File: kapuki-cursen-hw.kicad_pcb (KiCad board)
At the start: 2 copper layers, 27 parts, among them J1 Conn_01x02, J2 Conn_01x02, J3 Conn_01x01, J4 Conn_01x01, J5 Conn_01x01, J6 Conn_01x01, J7 Conn_01x06, J8 Conn_01x05, U1 MIC5235, U2 MAX4081S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

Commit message: Routing rev.1
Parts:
- removed the R5 at (154.5, 91.3)
- added D3: LED, LED_SMD:LED_0402_1005Metric, F.Cu at (139.5, 61.9)
- added D4: BZT52H-C3V3, Diode_SMD:D_SOD-123F, F.Cu at (130.2, 66.5)
- added R3: R, Resistor_SMD:R_0402_1005Metric, F.Cu at (139.0, 63.6)
- added R6: R, Resistor_SMD:R_0402_1005Metric, F.Cu at (141.0, 65.0)
- added REF**: OSHW-Logo2_7.3x6mm_SilkScreen, Symbol:OSHW-Logo2_7.3x6mm_SilkScreen, F.Cu at (125.9, 55.8)
- R2: footprint Resistor_SMD:R_0201_0603Metric -> Resistor_SMD:R_0402_1005Metric
- R4: renamed from R3; footprint Resistor_SMD:R_0201_0603Metric -> Resistor_SMD:R_0402_1005Metric
- R5: renamed from R4; footprint Resistor_SMD:R_0201_0603Metric -> Resistor_SMD:R_0402_1005Metric
- moved C5 37.4 mm to (129.7, 61.7), turned to 90 degrees
- moved R5 34.7 mm to (143.5, 63.4), turned to 270 degrees
- moved C4 32.9 mm to (130.8, 61.7), turned to 90 degrees
- moved R4 29.7 mm to (143.5, 66.0), turned to 270 degrees
- moved C7 29.7 mm to (135.9, 67.7), turned to 180 degrees
- moved FB1 29.0 mm to (137.4, 68.8)
- moved D2 28.5 mm to (134.4, 59.2)
- moved C3 27.7 mm to (133.0, 57.4)
- moved R2 27.7 mm to (136.3, 57.4)
- moved U2 27.6 mm to (134.6, 55.0)
- moved C8 27.5 mm to (135.4, 68.8), turned to 180 degrees
- moved J5 26.6 mm to (146.2, 62.9)
- moved C6 26.2 mm to (138.4, 66.1), turned to 270 degrees
- moved J1 25.6 mm to (124.5, 54.4), turned to 0 degrees
- moved J2 25.6 mm to (144.8, 54.4), turned to 0 degrees
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- renumbered J3 to Je
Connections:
- net /VCC renamed VCC
- C7 pad 1: Net-(C7-Pad1) -> /VCCA
- C8 pad 1: Net-(C7-Pad1) -> /VCCA
- FB1 pad 1: Net-(C7-Pad1) -> /VCCA
- R1 pad 3: (no net) -> Net-(R1-Pad3)
- R1 pad 4: (no net) -> Net-(J2-Pad2)
- U3 pad 15: Net-(U3-Pad15) -> /VCCA
- U3 pad 21: Net-(U3-Pad21) -> /LED
- U3 pad 23: Net-(U3-Pad23) -> /SWCLK
- U3 pad 24: /SWCLK -> /SWDIO
- U3 pad 25: /SWDIO -> Net-(U3-Pad25)
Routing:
- net VCC: track 0.00 -> 41.7 mm, vias 0 -> 3
- net /CURRMEAS: track 0.00 -> 29.3 mm, vias 0 -> 2
- net /VREF: track 0.00 -> 27.1 mm, vias 0 -> 2
- net GND: track 0.00 -> 23.6 mm, vias 0 -> 8
- net Net-(D4-Pad1): track 0.00 -> 21.8 mm, vias 0 -> 2
- net /SWDIO: track 0.00 -> 21.6 mm, vias 0 -> 2
- net /SWCLK: track 0.00 -> 20.0 mm, vias 0 -> 2
- net /MOTORPULSE: track 0.00 -> 14.9 mm
- net /VCCIN: track 0.00 -> 13.2 mm
- net /RXTX: track 0.00 -> 12.1 mm
- net /EXT6: track 0.00 -> 9.47 mm
- net /EXT5: track 0.00 -> 8.35 mm
- net /EXT1: track 0.00 -> 7.60 mm
- net /EXT2: track 0.00 -> 6.39 mm
- net /EXT4: track 0.00 -> 6.34 mm
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- added copper zone on B.Cu, net GND
- added copper zone on F.Cu, net GND
- added copper zone on B.Cu, net Net-(J1-Pad2)
- added copper zone on B.Cu, net Net-(J2-Pad2)
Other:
- board outline added: 26.9 x 26.5 mm
- net class Default: clearance 0.2 -> 0.1524; trace_width 0.25 -> 0.1524; via_dia 0.8 -> 0.6858; via_drill 0.4 -> 0.3302
- net class VCC added: clearance 0.2032, trace_width 0.254, via_dia 0.6858, via_drill 0.3302
- rule pad_to_mask_clearance: 0.051 -> 0.0508
- rule solder_mask_min_width: 0.25 -> 0.0508
- rule trace_clearance: 0.2 -> 0.1524
- rule trace_min: 0.2 -> 0.1524
- rule via_min_drill: 0.3 -> 0.3302
- rule via_min_size: 0.4 -> 0.6858
- board text added: "SWD"

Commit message: Send to OSHPark
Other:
- board text added: "Current Sensor rev.1 1946"
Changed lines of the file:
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@@
   (general
     (thickness 1.6)
-    (drawings 8)
+    (drawings 9)
     (tracks 222)
     (zones 0)
@@
     (visible_elements FFFFFF7F)
     (pcbplotparams
-      (layerselection 0x010fc_ffffffff)
+      (layerselection 0x010f0_ffffffff)
       (usegerberextensions false)
       (usegerberattributes false)
@@
       (outputformat 1)
       (mirror false)
-      (drillshape 1)
+      (drillshape 0)
       (scaleselection 1)
-      (outputdirectory ""))
+      (outputdirectory "gerber/"))
   )
   (net 0 "")
@@
       (net 2 GND))
   )
+  (gr_text "Current Sensor rev.1 1946" (at 134.62 49.911) (layer F.SilkS)
+    (effects (font (size 1 1) (thickness 0.15)))
+  )
   (dimension 26.543 (width 0.15) (layer Dwgs.User)

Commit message: Rev. 2
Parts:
- removed D2, D4: BZT52H-C3V3, Diode_SMD:D_SOD-123F
- removed J4, J5, Je: Conn_01x01, Connector_PinSocket_2.54mm:PinSocket_1x01_P2.54mm_Vertical
- removed REF**: OSHW-Logo2_7.3x6mm_SilkScreen, Symbol:OSHW-Logo2_7.3x6mm_SilkScreen
- added C10: 2.2uF, Capacitor_SMD:C_0402_1005Metric, F.Cu at (139.5, 63.3)
- added C11: 100nF, Capacitor_SMD:C_0402_1005Metric, F.Cu at (130.4, 59.9)
- added C9: 100nF, Capacitor_SMD:C_0402_1005Metric, F.Cu at (142.3, 61.7)
- added J3: Conn_01x03, Connector_PinHeader_2.54mm:PinHeader_1x03_P2.54mm_Vertical, F.Cu at (145.9, 62.9)
- added R7: 50, Resistor_SMD:R_0402_1005Metric, F.Cu at (137.9, 64.4)
- added R8: 10k, Resistor_SMD:R_0402_1005Metric, F.Cu at (132.8, 56.7)
- added U4: MCP1501, Package_TO_SOT_SMD:SOT-23-6, F.Cu at (142.0, 64.2)
- C3: value C -> 100pF
- C8: value 100nF -> 10nF
- FB1: value Ferrite_Bead -> 120ohm GHz
- R1: value R_Shunt -> 0.0002 1% 12W
- R2: value R -> 1k
- R4: value R -> 38k3 0.1%
- R5: value R -> 2k4 0.1%
- moved R4 19.6 mm to (128.1, 53.9), turned to 90 degrees
- moved R5 16.9 mm to (128.0, 56.5), turned to 90 degrees
- moved J6 11.1 mm to (128.4, 61.8)
- moved R6 5.21 mm to (141.0, 59.8)
- moved J7 3.68 mm to (141.0, 67.9)
- moved C4 3.34 mm to (130.5, 58.4)
- moved C5 3.31 mm to (129.4, 58.4)
- moved C6 3.30 mm to (138.4, 62.8)
- moved C7 3.30 mm to (135.9, 64.4)
- moved C8 3.30 mm to (135.4, 65.5)
- moved FB1 3.30 mm to (137.4, 65.5), turned to 180 degrees
- moved D3 3.30 mm to (139.5, 58.6)
- moved R3 3.30 mm to (139.0, 60.3)
- moved U3 3.30 mm to (134.6, 60.6)
- moved D1 2.51 mm to (128.8, 64.9), turned to 0 degrees
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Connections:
- net /CURRMEAS renamed /IMEAS
- net /LED renamed Net-(R3-Pad1)
- C1 pad 1: /VCCIN -> VCC
- C2 pad 1: VCC -> +3V3
- C4 pad 1: VCC -> +3V3
- C5 pad 1: VCC -> +3V3
- C6 pad 1: VCC -> +3V3
- C7 pad 1: /VCCA -> VDDA
- C8 pad 1: /VCCA -> VDDA
- D3 pad 2: VCC -> +3V3
- FB1 pad 1: /VCCA -> Net-(FB1-Pad1)
- FB1 pad 2: VCC -> VDDA
- J7 pad 1: /EXT6 -> GND
- J8 pad 1: /NRESET -> +3V3
- J8 pad 2: /SWDIO -> /SWCLK
- J8 pad 4: /SWCLK -> /SWDIO
- J8 pad 5: VCC -> /~RESET~
- R4 pad 1: Net-(D4-Pad1) -> /UMEAS
- R4 pad 2: /VCCIN -> Net-(J1-Pad2)
- R5 pad 2: Net-(D4-Pad1) -> /UMEAS
- R6 pad 2: VCC -> +3V3
- U1 pad 1: /VCCIN -> VCC
- U1 pad 3: /VCCIN -> VCC
- U1 pad 5: VCC -> +3V3
- U2 pad 2: Net-(J1-Pad2) -> VCC
- U3 pad 1: VCC -> +3V3
- U3 pad 10: /EXT2 -> /EXT1
- U3 pad 11: /EXT3 -> /EXT2
- U3 pad 12: /EXT4 -> /EXT3
- U3 pad 13: /EXT5 -> /EXT4
- U3 pad 15: /VCCA -> VDDA
- U3 pad 17: VCC -> +3V3
- U3 pad 18: /EXT6 -> /EXT5
- U3 pad 4: Net-(U3-Pad4) -> /~RESET~
- U3 pad 7: Net-(D4-Pad1) -> Net-(U3-Pad7)
- U3 pad 8: /EXT1 -> /UMEAS
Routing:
- net +3V3: track 0.00 -> 47.1 mm, vias 0 -> 2
- net Net-(D4-Pad1): track 21.8 -> 0.00 mm, vias 2 -> 0
- net /IMEAS: track 29.3 -> 11.5 mm
- net VCC: track 41.7 -> 25.6 mm, vias 3 -> 1
- net /VCCIN: track 13.2 -> 0.00 mm
- net /VREF: track 27.1 -> 14.1 mm
- net /UMEAS: track 0.00 -> 11.6 mm, vias 0 -> 2
- net /~RESET~: track 0.00 -> 9.86 mm
- net /EXT6: track 9.47 -> 0.00 mm
- net /MOTORPULSE: track 14.9 -> 7.88 mm
- net VDDA: track 0.00 -> 4.83 mm
- net Net-(FB1-Pad1): track 0.00 -> 4.39 mm
- net /VCCA: track 3.79 -> 0.00 mm
- net Net-(J1-Pad2): track 5.57 -> 2.39 mm, vias 1 -> 31
- net /SWCLK: track 20.0 -> 22.7 mm
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- added copper zone on F.Cu, net Net-(J1-Pad2)
- added copper zone on F.Cu, net Net-(J2-Pad2)
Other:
- board size 26.9 x 26.5 mm -> 26.9 x 23.1 mm

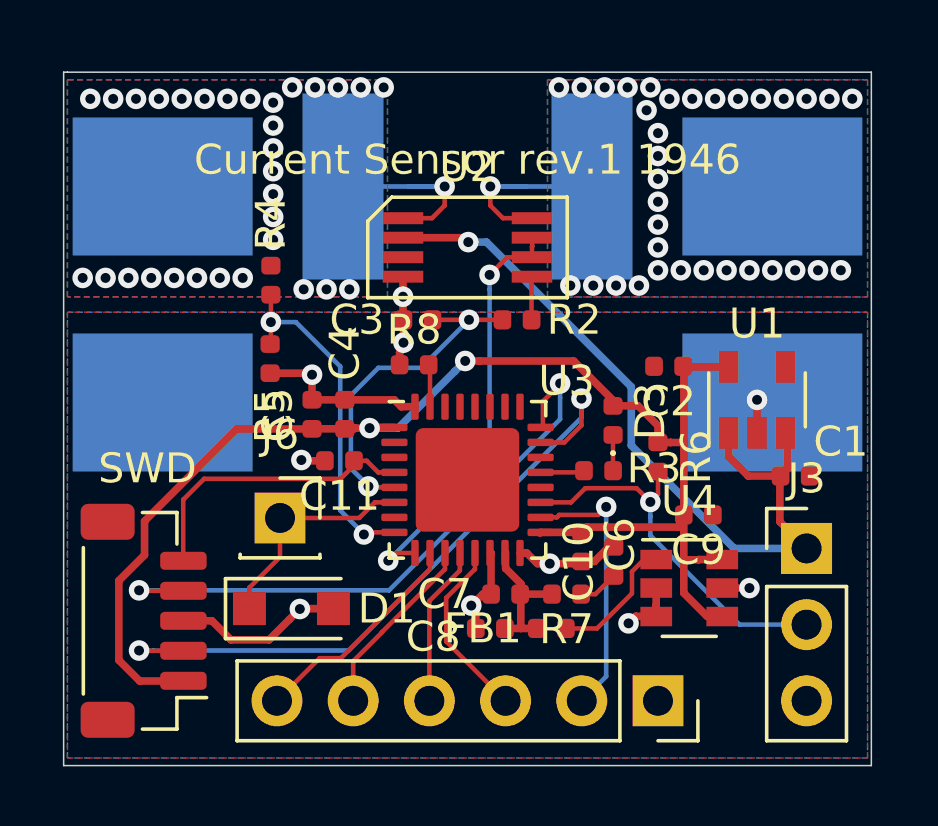
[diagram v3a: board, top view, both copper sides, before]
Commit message: Add precision voltage reference
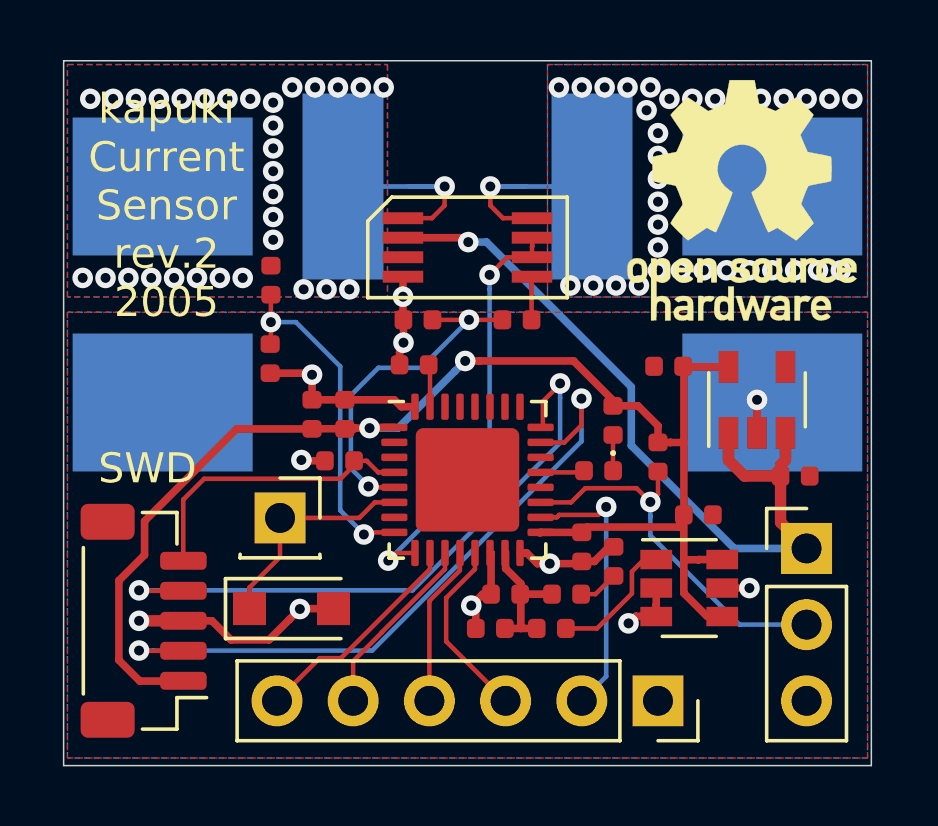
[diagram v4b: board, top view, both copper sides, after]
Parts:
- added REF**: OSHW-Logo_7.5x8mm_SilkScreen, Symbol:OSHW-Logo_7.5x8mm_SilkScreen, F.Cu at (143.8, 51.3)
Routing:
- net GND: track 25.9 -> 27.4 mm, vias 10 -> 11
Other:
- board size 26.9 x 23.1 mm -> 26.9 x 23.5 mm
- net class VCC: trace_width 0.254 -> 0.381
- board text added: "kapuki Current Sensor rev.2 2005"
- board text removed: "Current Sensor rev.1 1946"

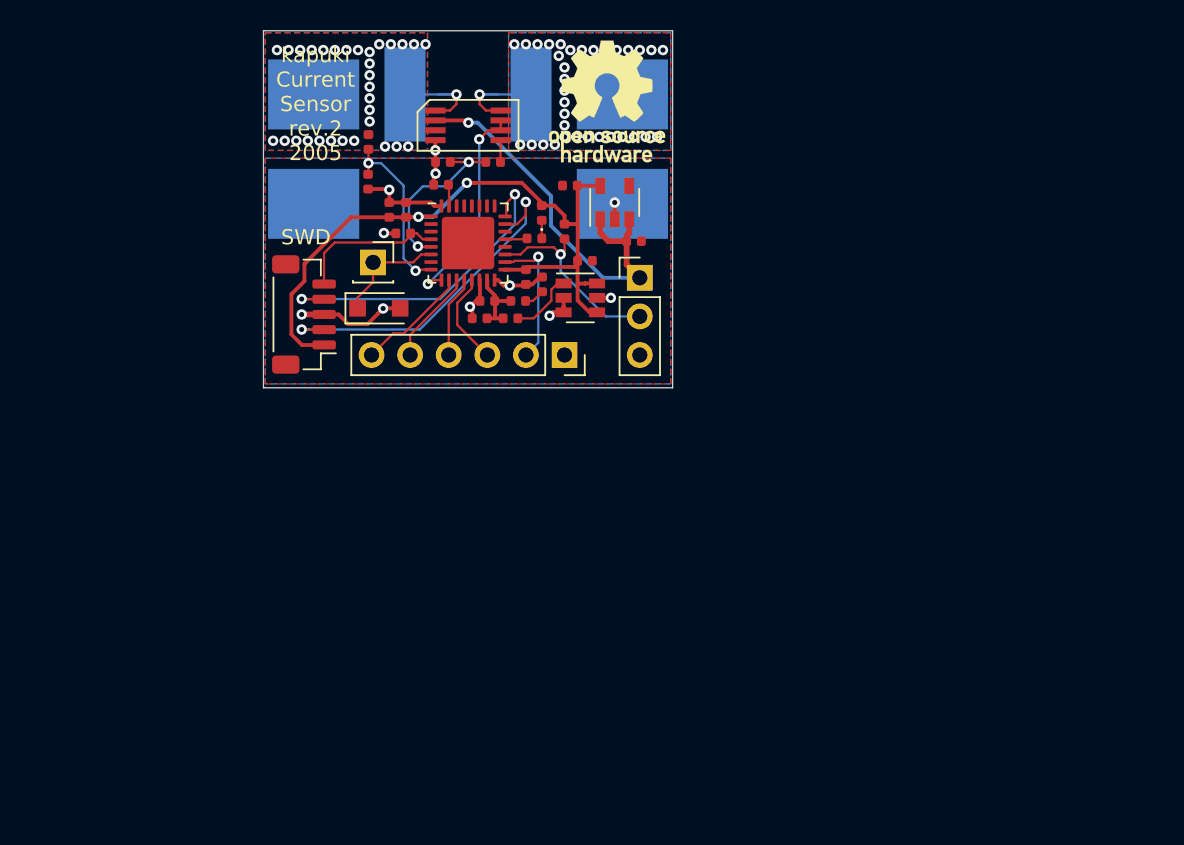
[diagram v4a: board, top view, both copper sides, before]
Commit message: Start the rev. 4 PCb design
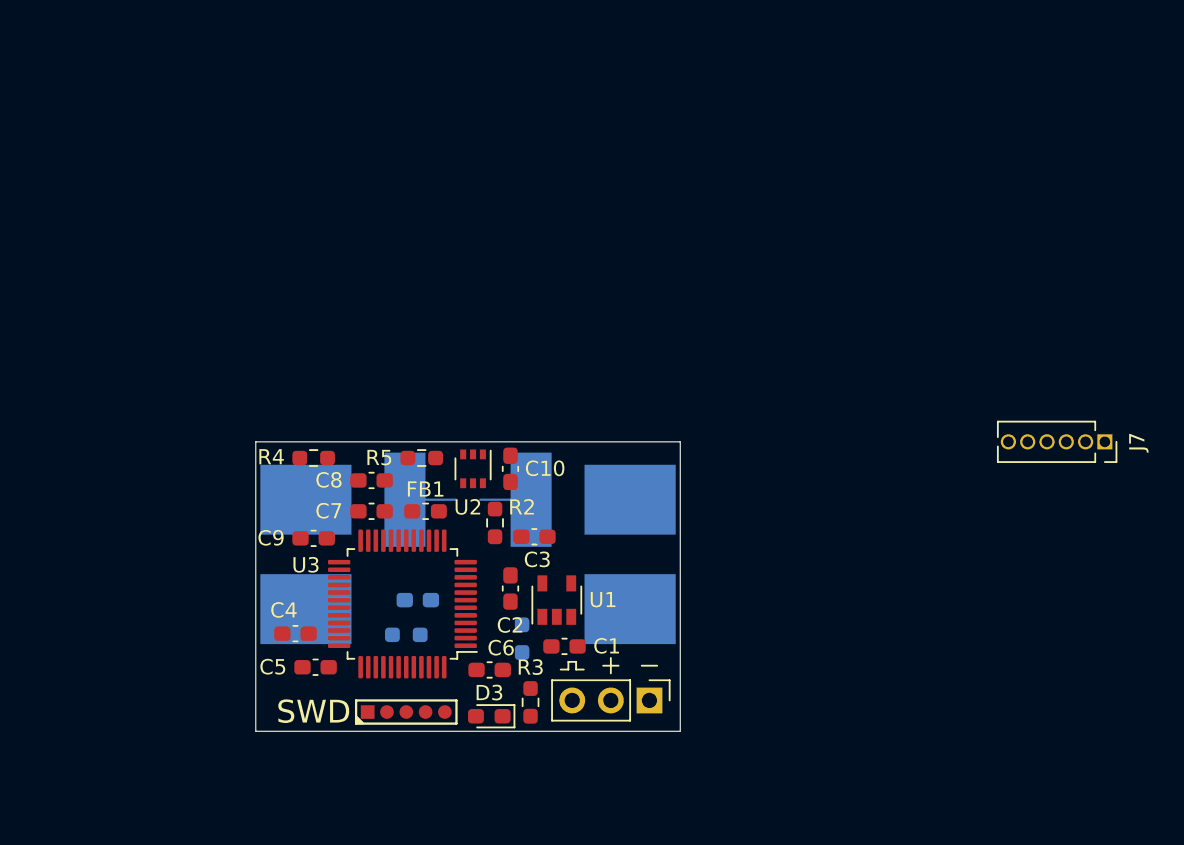
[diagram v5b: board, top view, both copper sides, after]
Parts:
- removed D1: BZT52H-C3V3, Diode_SMD:D_SOD-123F
- removed J6: Conn_01x01, Connector_PinSocket_2.54mm:PinSocket_1x01_P2.54mm_Vertical
- removed R7: 50, Resistor_SMD:R_0402_1005Metric
- removed REF**: OSHW-Logo_7.5x8mm_SilkScreen, Symbol:OSHW-Logo_7.5x8mm_SilkScreen
- removed U4: MCP1501, Package_TO_SOT_SMD:SOT-23-6
- C1, C2, C3, C4, C5, C6, C7, C8, C9: footprint Capacitor_SMD:C_0402_1005Metric -> Capacitor_SMD:C_0603_1608Metric_Pad1.08x0.95mm_HandSolder
- C10: value 2.2uF -> 100n; footprint Capacitor_SMD:C_0402_1005Metric -> Capacitor_SMD:C_0603_1608Metric_Pad1.08x0.95mm_HandSolder
- C11: footprint Capacitor_SMD:C_0402_1005Metric -> Capacitor_SMD:C_0603_1608Metric_Pad1.08x0.95mm_HandSolder; moved to B.Cu
- D3: footprint LED_SMD:LED_0402_1005Metric -> LED_SMD:LED_0603_1608Metric_Pad1.05x0.95mm_HandSolder
- FB1: value 120ohm GHz -> 100 @ 100MHz; footprint Resistor_SMD:R_0402_1005Metric -> Inductor_SMD:L_0603_1608Metric_Pad1.05x0.95mm_HandSolder
- J7: footprint Connector_PinSocket_2.54mm:PinSocket_1x06_P2.54mm_Vertical -> Connector_PinSocket_1.27mm:PinSocket_1x06_P1.27mm_Vertical
- J8: footprint Connector_JST:JST_SH_BM05B-SRSS-TB_1x05-1MP_P1.00mm_Vertical -> local:TestPoint_5Pad_D0.8mm
- R1: value 0.0002 1% 12W -> 0.0002ohm 1% 12W
- R2: footprint Resistor_SMD:R_0402_1005Metric -> Resistor_SMD:R_0603_1608Metric_Pad0.98x0.95mm_HandSolder
- R3: value R -> 1k; footprint Resistor_SMD:R_0402_1005Metric -> Resistor_SMD:R_0603_1608Metric_Pad0.98x0.95mm_HandSolder
- R4: value 38k3 0.1% -> 18k 1%; footprint Resistor_SMD:R_0402_1005Metric -> Resistor_SMD:R_0603_1608Metric_Pad0.98x0.95mm_HandSolder
- R5: value 2k4 0.1% -> 2k4 1%; footprint Resistor_SMD:R_0402_1005Metric -> Resistor_SMD:R_0603_1608Metric_Pad0.98x0.95mm_HandSolder
- R6: value R -> 4k7; footprint Resistor_SMD:R_0402_1005Metric -> Resistor_SMD:R_0603_1608Metric_Pad0.98x0.95mm_HandSolder; moved to B.Cu
- R8: footprint Resistor_SMD:R_0402_1005Metric -> Resistor_SMD:R_0603_1608Metric_Pad0.98x0.95mm_HandSolder; moved to B.Cu
- U2: value MAX4081S -> INA199; footprint local:uMAX-8 -> Package_TO_SOT_SMD:SOT-363_SC-70-6
- U3: value STM32G431KBUx -> STM32G431CBTx; footprint Package_DFN_QFN:QFN-32-1EP_5x5mm_P0.5mm_EP3.45x3.45mm -> Package_QFP:LQFP-48_7x7mm_P0.5mm
- moved J7 36.0 mm to (176.5, 73.7)
- moved D3 33.3 mm to (136.0, 91.7), turned to 180 degrees
- moved R3 30.5 mm to (138.7, 90.8), turned to 270 degrees
- moved C5 30.5 mm to (124.6, 88.5), turned to 180 degrees
- moved R8 29.7 mm to (130.6, 86.4)
- moved C4 28.8 mm to (123.3, 86.3), turned to 180 degrees
- moved J3 27.8 mm to (146.6, 90.7), turned to 270 degrees
- moved C1 27.1 mm to (141.0, 87.1), turned to 180 degrees
- moved R6 26.9 mm to (138.2, 86.6), turned to 270 degrees
- moved C2 26.8 mm to (137.4, 83.3), turned to 270 degrees
- moved J1 26.7 mm to (124.0, 81.1)
- moved J2 26.7 mm to (145.3, 81.1)
- moved R1 26.7 mm to (134.6, 77.5)
- moved J8 26.5 mm to (128.0, 91.4), turned to 0 degrees
- moved U1 26.4 mm to (140.5, 84.1)
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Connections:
- C10 pad 1: Net-(C10-Pad1) -> GND
- C10 pad 2: GND -> VCC
- C9 pad 1: GND -> +3V3
- C9 pad 2: +3V3 -> GND
- FB1 pad 1: Net-(FB1-Pad1) -> VDDA
- FB1 pad 2: VDDA -> +3V3
- J3 pad 1: VCC -> GND
- J3 pad 2: /RXTX -> VCC
- J3 pad 3: GND -> /RXTX
- U2 pad 1: Net-(R1-Pad2) -> /REF
- U2 pad 2: VCC -> GND
- U2 pad 3: Net-(U2-Pad3) -> VCC
- U2 pad 4: GND -> Net-(R1-Pad2)
- U2 pad 5: Net-(R2-Pad2) -> Net-(R1-Pad3)
- U2 pad 6: /VREF -> Net-(R2-Pad2)
- U3 pad 1: +3V3 -> Net-(U3-Pad1)
- U3 pad 10: /EXT1 -> /RXTX
- U3 pad 11: /EXT2 -> Net-(U3-Pad11)
- U3 pad 12: /EXT3 -> Net-(U3-Pad12)
- U3 pad 13: /EXT4 -> /REF
- U3 pad 14: GND -> Net-(U3-Pad14)
- U3 pad 15: VDDA -> Net-(U3-Pad15)
- U3 pad 16: GND -> /IMEAS
- U3 pad 17: +3V3 -> Net-(U3-Pad17)
- U3 pad 18: /EXT5 -> /UMEAS
- U3 pad 19: /RXTX -> GND
- U3 pad 21: Net-(R3-Pad1) -> VDDA
- U3 pad 23: /SWCLK -> GND
- U3 pad 24: /SWDIO -> +3V3
- U3 pad 31: Net-(R8-Pad2) -> /TX
- U3 pad 32: GND -> /RX
- U3 pad 33: (no net) -> Net-(U3-Pad33)
- U3 pad 4: /~RESET~ -> Net-(U3-Pad4)
- U3 pad 5: /IMEAS -> Net-(U3-Pad5)
- U3 pad 6: /MOTORPULSE -> Net-(U3-Pad6)
- U3 pad 7: Net-(U3-Pad7) -> /~RESET~
- U3 pad 8: /UMEAS -> Net-(R3-Pad1)
- U3 pad 9: /VREF -> Net-(U3-Pad9)
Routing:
- net +3V3: track 47.1 -> 0.00 mm, vias 2 -> 0
- net GND: track 27.4 -> 0.00 mm, vias 11 -> 0
- net VCC: track 26.1 -> 0.00 mm, vias 1 -> 0
- net /SWCLK: track 23.1 -> 0.00 mm, vias 2 -> 0
- net /SWDIO: track 21.2 -> 0.00 mm, vias 2 -> 0
- net /VREF: track 14.1 -> 0.00 mm, vias 2 -> 0
- net /RXTX: track 13.1 -> 0.00 mm, vias 1 -> 0
- net /UMEAS: track 11.6 -> 0.00 mm, vias 2 -> 0
- net /IMEAS: track 11.5 -> 0.00 mm, vias 2 -> 0
- net /~RESET~: track 9.86 -> 0.00 mm
- net /EXT5: track 9.13 -> 0.00 mm, vias 1 -> 0
- net /MOTORPULSE: track 7.88 -> 0.00 mm
- net /EXT1: track 7.45 -> 0.00 mm
- net /EXT2: track 6.20 -> 0.00 mm
- net /EXT4: track 6.15 -> 0.00 mm
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- removed copper zone on B.Cu, net GND
- removed copper zone on F.Cu, net GND
- removed copper zone on B.Cu, net Net-(J1-Pad2)
- removed copper zone on F.Cu, net Net-(J1-Pad2)
- removed copper zone on B.Cu, net Net-(J2-Pad2)
- removed copper zone on F.Cu, net Net-(J2-Pad2)
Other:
- board size 26.9 x 23.5 mm -> 27.9 x 19 mm
- copper layers 2 -> 4
- board text added: "kapuki-CS"
- board text added: "rev. 4 2106"
- board text removed: "kapuki Current Sensor rev.2 2005"
